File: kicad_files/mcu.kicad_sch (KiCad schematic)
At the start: 1 part

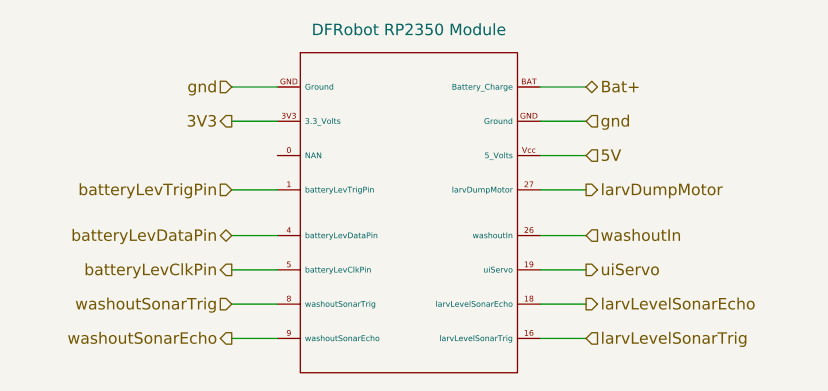
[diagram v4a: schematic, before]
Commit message: ERC errors cleaned. Hierarchical wiring finished. PWM converter change. Motor driver change.
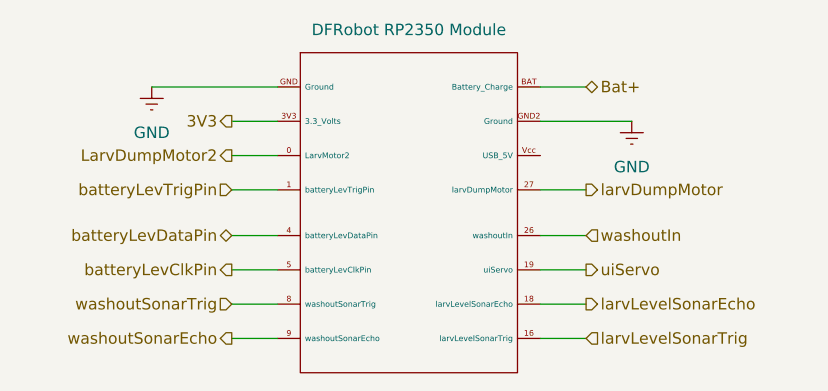
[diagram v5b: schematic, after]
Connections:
- net LarvDumpMotor2: now reaches .1.0 (LarvMotor2)
- net 5V: no longer names the net of .1.Vcc (USB_5V)
- net gnd renamed GND
- net GND: now also .1.GND2 (Ground)
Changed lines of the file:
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@@
 	(wire
 		(pts
-			(xy 163.83 90.17) (xy 168.91 90.17)
+			(xy 129.54 102.87) (xy 134.62 102.87)
+		)
+		(stroke
+			(width 0)
+			(type default)
+			(color 183 13 255 1)
+		)
+	)
+	(wire
+		(pts
+			(xy 129.54 106.68) (xy 134.62 106.68)
+		)
+		(stroke
+			(width 0)
+			(type default)
+			(color 183 13 255 1)
+		)
+	)
+	(wire
+		(pts
+			(xy 129.54 114.3) (xy 134.62 114.3)
+		)
+		(stroke
+			(width 0)
+			(type default)
+			(color 7 4 255 1)
+		)
+	)
+	(wire
+		(pts
+			(xy 129.54 93.98) (xy 134.62 93.98)
+		)
+		(stroke
+			(width 0)
+			(type default)
+		)
+	)
+	(wire
+		(pts
+			(xy 163.83 106.68) (xy 168.91 106.68)
+		)
+		(stroke
+			(width 0)
+			(type default)
+			(color 255 190 4 1)
+		)
+	)
+	(wire
+		(pts
+			(xy 129.54 90.17) (xy 134.62 90.17)
+		)
+		(stroke
+			(width 0)
+			(type default)
+			(color 255 159 7 1)
+		)
+	)
+	(wire
+		(pts
+			(xy 163.83 102.87) (xy 168.91 102.87)
+		)
+		(stroke
+			(width 0)
+			(type default)
+			(color 194 189 255 1)
+		)
+	)
+	(wire
+		(pts
+			(xy 129.54 110.49) (xy 134.62 110.49)
+		)
+		(stroke
+			(width 0)
+			(type default)
+			(color 7 4 255 1)
+		)
+	)
+	(wire
+		(pts
+			(xy 120.65 86.36) (xy 134.62 86.36)
 		)
 		(stroke
@@
 	(wire
 		(pts
-			(xy 129.54 102.87) (xy 134.62 102.87)
-		)
-		(stroke
-			(width 0)
-			(type default)
-			(color 183 13 255 1)
-		)
-	)
-	(wire
-		(pts
-			(xy 129.54 106.68) (xy 134.62 106.68)
-		)
-		(stroke
-			(width 0)
-			(type default)
-			(color 183 13 255 1)
-		)
-	)
-	(wire
-		(pts
-			(xy 129.54 114.3) (xy 134.62 114.3)
-		)
-		(stroke
-			(width 0)
-			(type default)
-			(color 7 4 255 1)
-		)
-	)
-	(wire
-		(pts
-			(xy 163.83 93.98) (xy 168.91 93.98)
-		)
-		(stroke
-			(width 0)
-			(type default)
-			(color 255 7 11 1)
-		)
-	)
-	(wire
-		(pts
-			(xy 163.83 106.68) (xy 168.91 106.68)
-		)
-		(stroke
-			(width 0)
-			(type default)
-			(color 255 190 4 1)
-		)
-	)
-	(wire
-		(pts
-			(xy 129.54 90.17) (xy 134.62 90.17)
-		)
-		(stroke
-			(width 0)
-			(type default)
-			(color 255 159 7 1)
-		)
-	)
-	(wire
-		(pts
-			(xy 163.83 102.87) (xy 168.91 102.87)
-		)
-		(stroke
-			(width 0)
-			(type default)
-			(color 194 189 255 1)
-		)
-	)
-	(wire
-		(pts
-			(xy 129.54 110.49) (xy 134.62 110.49)
-		)
-		(stroke
-			(width 0)
-			(type default)
-			(color 7 4 255 1)
-		)
-	)
-	(wire
-		(pts
-			(xy 129.54 86.36) (xy 134.62 86.36)
-		)
-		(stroke
-			(width 0)
-			(type default)
-			(color 0 0 0 1)
-		)
-	)
-	(wire
-		(pts
 			(xy 163.83 86.36) (xy 168.91 86.36)
 		)
@@
 			(type default)
 			(color 255 22 184 1)
+		)
+	)
+	(wire
+		(pts
+			(xy 163.83 90.17) (xy 173.99 90.17)
+		)
+		(stroke
+			(width 0)
+			(type default)
 		)
 	)
@@
 		)
 	)
+	(hierarchical_label "LarvDumpMotor2"
+		(shape output)
+		(at 129.54 93.98 180)
+		(effects
+			(font
+				(size 1.27 1.27)
+			)
+			(justify right)
+		)
+	)
 	(hierarchical_label "Bat+"
 		(shape bidirectional)
@@
 		)
 	)
-	(hierarchical_label "gnd"
-		(shape input)
-		(at 168.91 90.17 0)
-		(effects
-			(font
-				(size 1.27 1.27)
-			)
-			(justify left)
-		)
-	)
-	(hierarchical_label "gnd"
-		(shape input)
-		(at 129.54 86.36 180)
-		(effects
-			(font
-				(size 1.27 1.27)
-			)
-			(justify right)
-		)
-	)
 	(hierarchical_label "larvLevelSonarTrig"
 		(shape input)
@@
 		)
 	)
-	(hierarchical_label "5V"
-		(shape input)
-		(at 168.91 93.98 0)
-		(effects
-			(font
-				(size 1.27 1.27)
-			)
-			(justify left)
-		)
-	)
 	(hierarchical_label "batteryLevDataPin"
 		(shape bidirectional)
@@
 			)
 			(justify right)
+		)
+	)
+	(symbol
+		(lib_id "power:GNDREF")
+		(at 173.99 90.17 0)
+		(unit 1)
+		(exclude_from_sim no)
+		(in_bom yes)
+		(on_board yes)
+		(dnp no)
+		(fields_autoplaced yes)
+		(property "Reference" "#PWR09"
+			(at 173.99 96.52 0)
+			(effects
+				(font
+					(size 1.27 1.27)
+				)
+				(hide yes)
+			)
+		)
+		(property "Value" "GND"
+			(at 173.99 95.25 0)
+			(effects
+				(font
+					(size 1.27 1.27)
+				)
+			)
+		)
+		(property "Footprint" ""
+			(at 173.99 90.17 0)
+			(effects
+				(font
+					(size 1.27 1.27)
+				)
+				(hide yes)
+			)
+		)
+		(property "Datasheet" ""
+			(at 173.99 90.17 0)
+			(effects
+				(font
+					(size 1.27 1.27)
+				)
+				(hide yes)
+			)
+		)
+		(property "Description" "Power symbol creates a global label with name \"GNDREF\" , reference supply ground"
+			(at 173.99 90.17 0)
+			(effects
+				(font
+					(size 1.27 1.27)
+				)
+				(hide yes)
+			)
+		)
+		(pin "1"
+		)
+		(instances
+			(project "kicad_files"
+				(path "/67de3bec-6c8a-4e66-9cf7-9a8a92865209/ff56d200-a0c3-45b4-9685-fddfa8df3924"
+					(reference "#PWR09")
+					(unit 1)
+				)
+			)
 		)
 	)
@@
 		(pin "BAT"
 		)
-		(pin "GND"
+		(pin "GND2"
 		)
 		(pin "Vcc"
@@
 					(unit 1)
 				)
+			)
+		)
+	)
+	(symbol
+		(lib_id "power:GNDREF")
+		(at 120.65 86.36 0)
+		(unit 1)
+		(exclude_from_sim no)
+		(in_bom yes)
+		(on_board yes)
+		(dnp no)
+		(fields_autoplaced yes)
+		(property "Reference" "#PWR08"
+			(at 120.65 92.71 0)
+			(effects
+				(font
+					(size 1.27 1.27)
+				)
+				(hide yes)
+			)
+		)
+		(property "Value" "GND"
+			(at 120.65 91.44 0)
+			(effects
+				(font
+					(size 1.27 1.27)
+				)
+			)
+		)
+		(property "Footprint" ""
+			(at 120.65 86.36 0)
+			(effects
+				(font
+					(size 1.27 1.27)
+				)
+				(hide yes)
+			)
+		)
+		(property "Datasheet" ""
+			(at 120.65 86.36 0)
+			(effects
+				(font
+					(size 1.27 1.27)
+				)
+				(hide yes)
+			)
+		)
+		(property "Description" "Power symbol creates a global label with name \"GNDREF\" , reference supply ground"
+			(at 120.65 86.36 0)
+			(effects
+				(font
+					(size 1.27 1.27)
+				)
+				(hide yes)
+			)
+		)
+		(pin "1"
+		)
+		(instances
+			(project "kicad_files"
+				(path "/67de3bec-6c8a-4e66-9cf7-9a8a92865209/ff56d200-a0c3-45b4-9685-fddfa8df3924"
+					(reference "#PWR08")
+					(unit 1)
+				)

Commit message: Footprint assignment finished
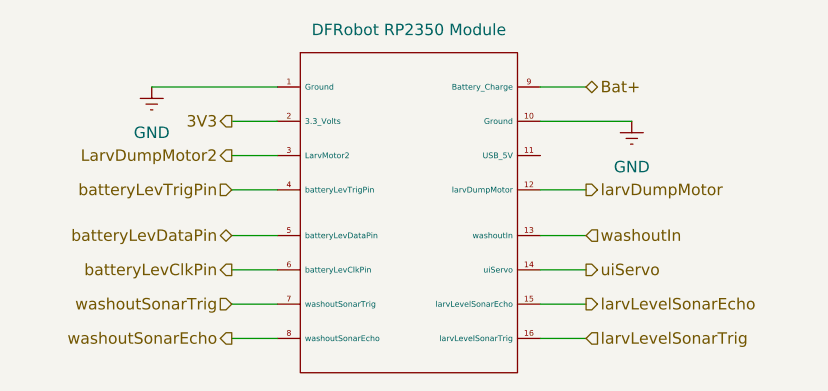
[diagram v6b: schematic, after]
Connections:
- net 3V3: now also .1.2 (3.3_Volts); no longer .1.3V3 (3.3_Volts)
- net Bat+: now also .1.9 (Battery_Charge); no longer .1.BAT (Battery_Charge)
- net GND: now also .1.1 (Ground), .1.10 (Ground); no longer .1.GND (Ground), .1.GND2 (Ground)
- net LarvDumpMotor2: now also .1.3 (LarvMotor2); no longer .1.0 (LarvMotor2)
- net batteryLevClkPin: now also .1.6 (batteryLevClkPin); no longer .1.5 (batteryLevClkPin)
- net batteryLevDataPin: now also .1.5 (batteryLevDataPin); no longer .1.4 (batteryLevDataPin)
- net batteryLevTrigPin: now also .1.4 (batteryLevTrigPin); no longer .1.1 (batteryLevTrigPin)
- net larvDumpMotor: now also .1.12 (larvDumpMotor); no longer .1.27 (larvDumpMotor)
- net larvLevelSonarEcho: now also .1.15 (larvLevelSonarEcho); no longer .1.18 (larvLevelSonarEcho)
- net uiServo: now also .1.14 (uiServo); no longer .1.19 (uiServo)
- net washoutIn: now also .1.13 (washoutIn); no longer .1.26 (washoutIn)
- net washoutSonarEcho: now also .1.8 (washoutSonarEcho); no longer .1.9 (washoutSonarEcho)
- net washoutSonarTrig: now also .1.7 (washoutSonarTrig); no longer .1.8 (washoutSonarTrig)
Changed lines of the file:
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@@
 			)
 		)
-		(pin "GND"
+		(pin "15"
 		)
 		(pin "4"
 		)
-		(pin "3V3"
+		(pin "2"
 		)
-		(pin "0"
+		(pin "13"
 		)
 		(pin "9"
@@
 		(pin "8"
 		)
-		(pin "BAT"
+		(pin "10"
 		)
-		(pin "GND2"
+		(pin "3"
 		)
-		(pin "Vcc"
+		(pin "11"
 		)
-		(pin "27"
+		(pin "12"
 		)
 		(pin "16"
 		)
-		(pin "26"
+		(pin "14"
 		)
-		(pin "18"
+		(pin "6"
 		)
-		(pin "19"
+		(pin "7"
 		)
 		(instances

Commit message: Schematic and Footprint error fix
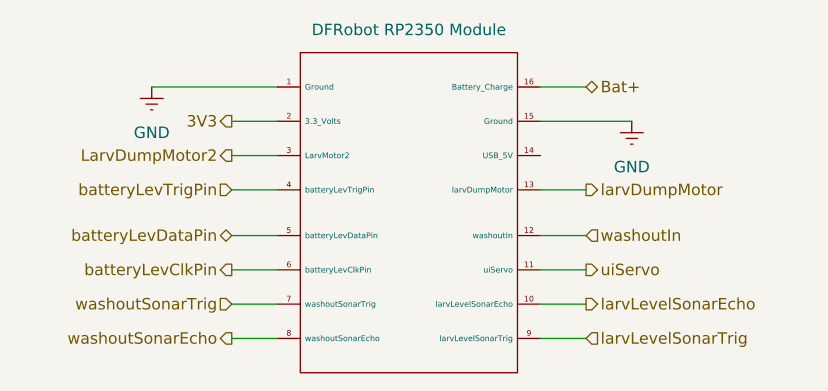
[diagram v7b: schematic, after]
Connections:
- net Bat+: now also .1.16 (Battery_Charge); no longer .1.9 (Battery_Charge)
- net GND: now also .1.15 (Ground); no longer .1.10 (Ground)
- net larvDumpMotor: now also .1.13 (larvDumpMotor); no longer .1.12 (larvDumpMotor)
- net larvLevelSonarEcho: now also .1.10 (larvLevelSonarEcho); no longer .1.15 (larvLevelSonarEcho)
- net larvLevelSonarTrig: now also .1.9 (larvLevelSonarTrig); no longer .1.16 (larvLevelSonarTrig)
- net uiServo: now also .1.11 (uiServo); no longer .1.14 (uiServo)
- net washoutIn: now also .1.12 (washoutIn); no longer .1.13 (washoutIn)
